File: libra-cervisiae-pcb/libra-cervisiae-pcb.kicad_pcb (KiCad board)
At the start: 2 copper layers, 63.8 x 43.2 mm, 161 parts, among them CN1 CP2102-BREAKOUT, CN3 HX711_BREAKOUT, J1 Board Temp, J10 Load Cell, J12 Load Cell, J4 Wort Temp, J8 Load Cell, J9 Load Cell, SW1 Reset, SW2 Flash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

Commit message: Versioning, silkscreen changes
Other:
- board text added: "0.1.0"
- board text added: "Load Cells"
- board text removed: "1.0.0"
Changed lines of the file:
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@@
   (general
     (thickness 1.6)
-    (drawings 12)
+    (drawings 14)
     (tracks 342)
     (zones 0)
@@
   (title_block
     (title "Libra Cervisiae PCB")
-    (date 2018-07-19)
-    (rev 1.0.0-rc.1)
+    (date 2018-07-23)
+    (rev 0.1.0)
   )
   (layers
@@
     (aux_axis_origin 11.938 11.938)
     (grid_origin 160.909 81.534)
-    (visible_elements FFFFFFFF)
+    (visible_elements FFFFEFFF)
     (pcbplotparams
       (layerselection 0x010fc_ffffffff)
@@
       (effects (font (size 1 1) (thickness 0.15)))
     )
-    (fp_text value "Load Cell" (at -9.779 -2.286 180) (layer F.SilkS)
+    (fp_text value "Load Cell" (at 1.8415 5.6515 180) (layer F.Fab)
       (effects (font (size 1 1) (thickness 0.15)))
     )
@@
     )
   )
+  (gr_line (start 139.954 88.025) (end 139.954 73.025) (angle 90) (layer F.SilkS) (width 0.2))
+  (gr_text "Load Cells" (at 136.017 69.723 90) (layer F.SilkS)
+    (effects (font (size 1 1) (thickness 0.15)))
+  )
   (gr_text "GRN/WHT +/-S\nBLK/RED -/+E" (at 152.908 59.309) (layer Cmts.User)
     (effects (font (size 1 1) (thickness 0.15)))
   )
   (gr_line (start 163.216 73.025) (end 139.954 73.025) (angle 90) (layer F.SilkS) (width 0.2))
-  (gr_line (start 163.195 88.152) (end 163.195 73.152) (angle 90) (layer F.SilkS) (width 0.2))
+  (gr_line (start 163.195 88.025) (end 163.195 73.025) (angle 90) (layer F.SilkS) (width 0.2))
   (dimension 64 (width 0.3) (layer Dwgs.User)
     (gr_text "64.000 mm" (at 138.138 59.988) (layer Dwgs.User)
@@
     (arrow2b (pts (xy 100.138 111.738) (xy 101.264504 111.151579)))
   )
-  (gr_text 1.0.0 (at 126.873 82.931) (layer F.SilkS)
+  (gr_text 0.1.0 (at 126.873 82.931) (layer F.SilkS)
     (effects (font (size 1 1) (thickness 0.15)))
   )

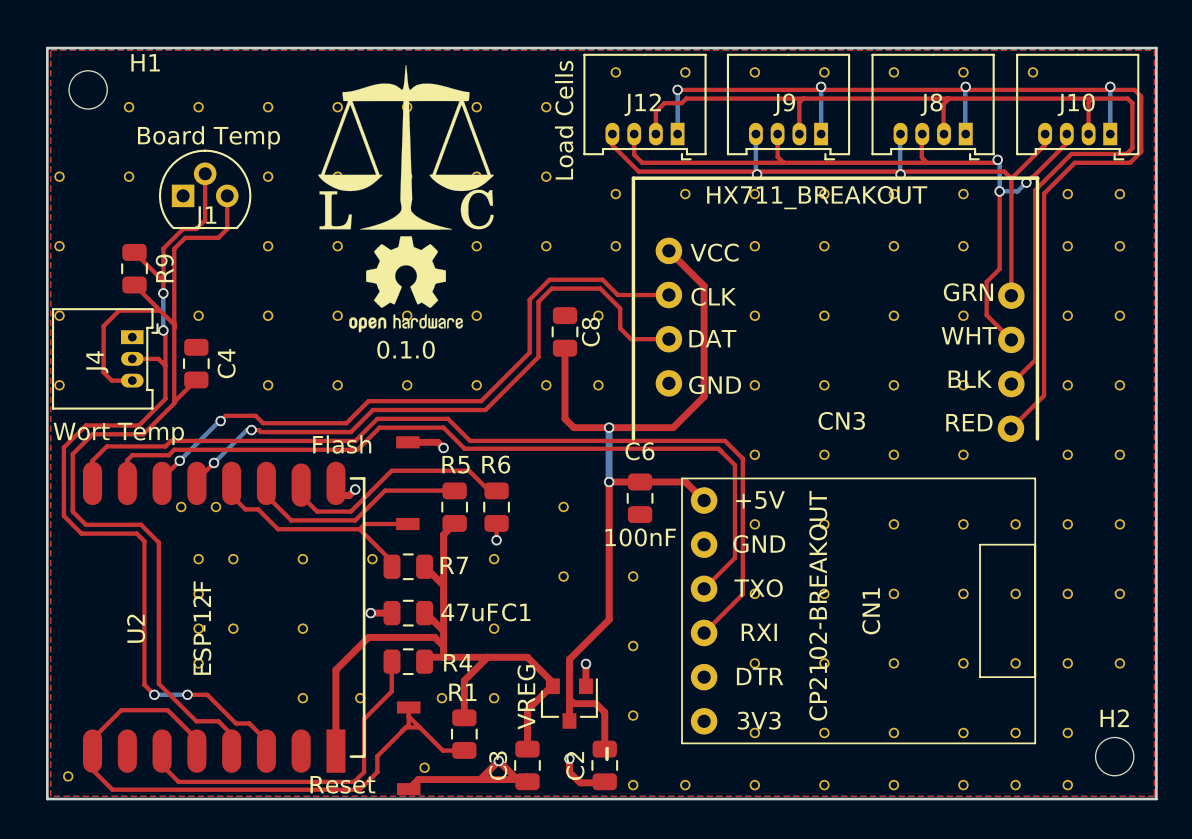
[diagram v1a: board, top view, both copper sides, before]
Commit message: Some PCB tweaks based on measuring the breakout boards
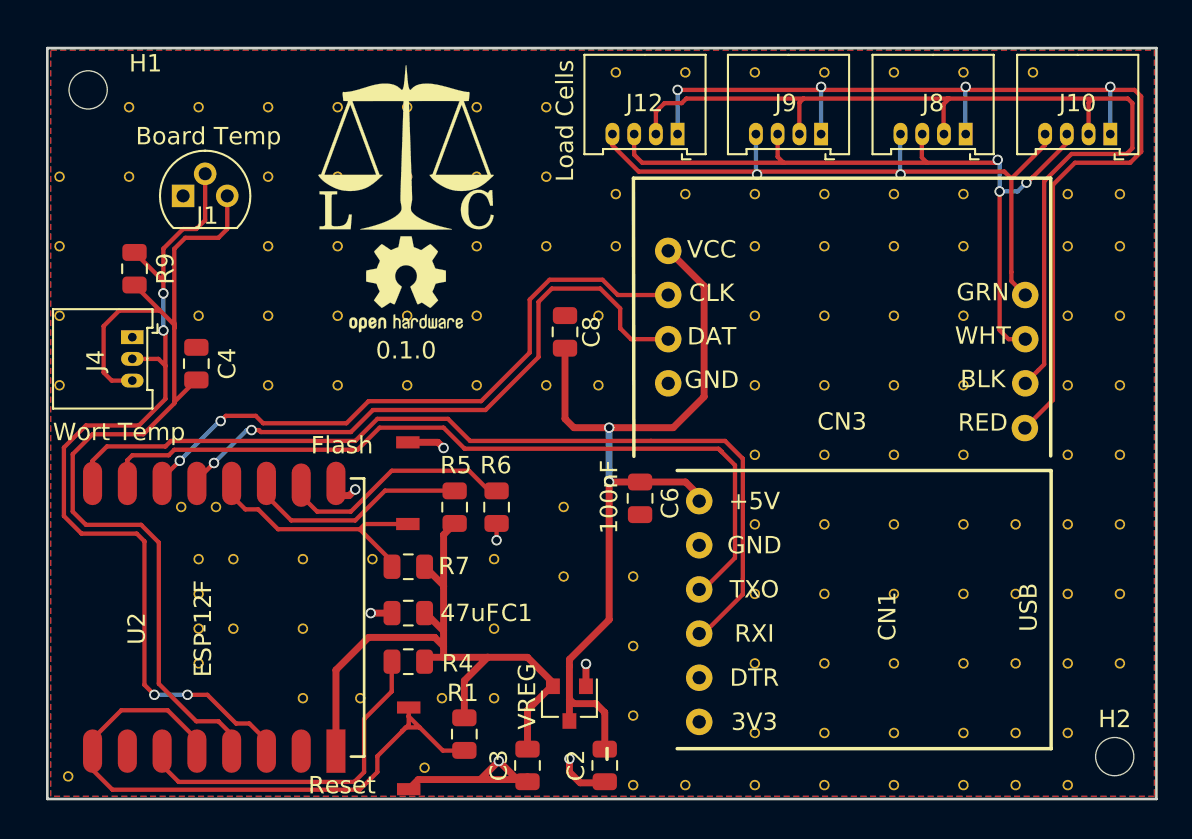
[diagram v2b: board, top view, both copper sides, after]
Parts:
- CN1: value CP2102-BREAKOUT -> CP2102
- moved CN1 0.94 mm to (164.0, 105.8)

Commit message: PCB cleanup (tracks, lines)
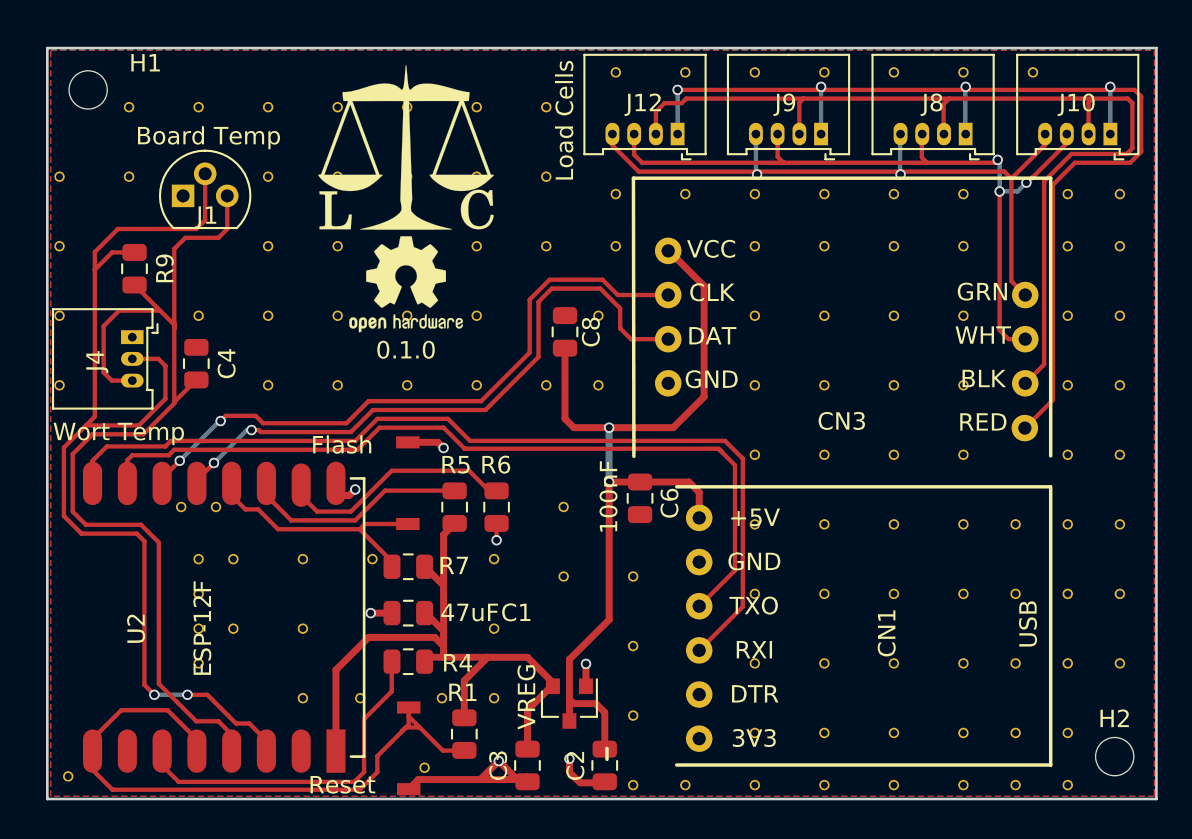
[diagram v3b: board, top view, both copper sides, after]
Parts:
- moved CN1 0.97 mm to (164.0, 106.8)
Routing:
- net /DSD: track 52.7 -> 60.5 mm, vias 4 -> 2
- net /HostRX: track 52.3 -> 53.4 mm
- net /HostTX: track 48.2 -> 49.3 mm
- net /USB+: track 50.5 -> 51.5 mm

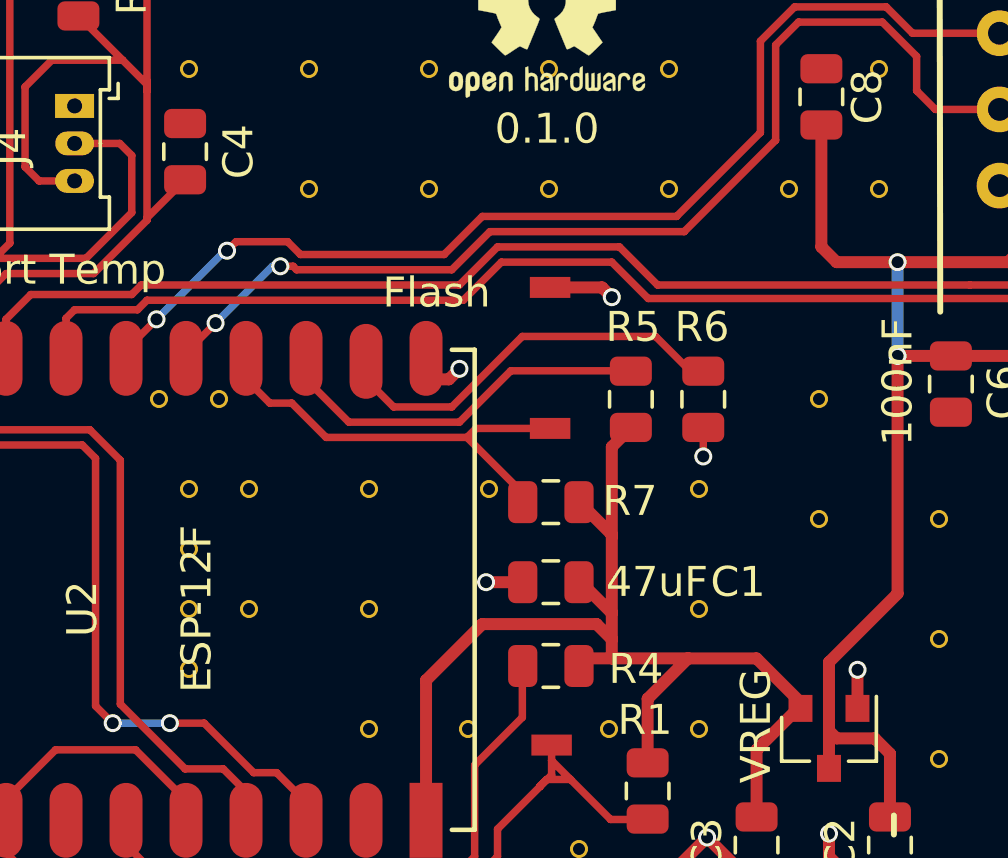
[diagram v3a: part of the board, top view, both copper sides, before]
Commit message: PCB stitching via tweaks
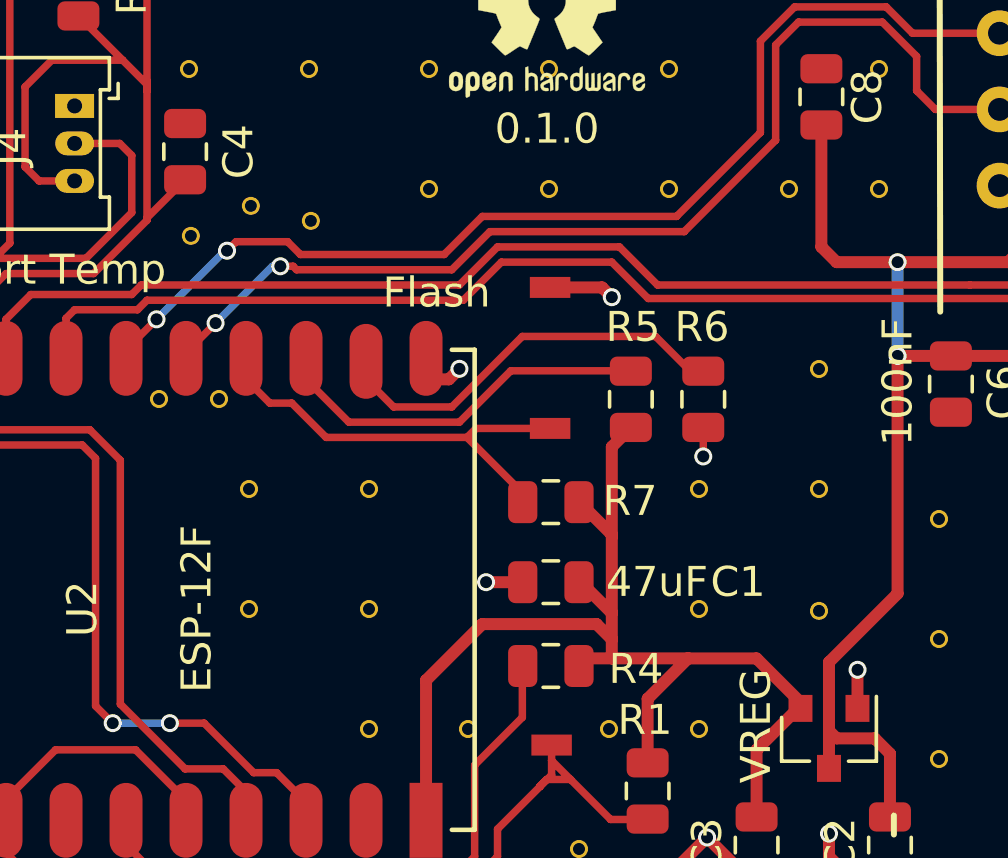
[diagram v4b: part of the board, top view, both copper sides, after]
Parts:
- removed the REF** at (124.9, 94.9)
- removed the REF** at (118.9, 84.9)
- removed the REF** at (114.9, 98.9)
- removed the REF** at (114.9, 100.9)
- removed the REF** at (114.9, 96.9)
- removed the REF** at (114.9, 94.9)
- added REF**: Stitch, Extra_Pads:Stitching_Via_0.6mm, F.Cu at (119.0, 86.0)
- added REF**: Stitch, Extra_Pads:Stitching_Via_0.6mm, F.Cu at (117.0, 85.5)
- added REF**: Stitch, Extra_Pads:Stitching_Via_0.6mm, F.Cu at (115.0, 86.5)
- added REF**: Stitch, Extra_Pads:Stitching_Via_0.6mm, F.Cu at (135.9, 99.0)
- moved REF** 1.00 mm to (135.9, 94.9)
- moved REF** 1.00 mm to (135.9, 90.9)
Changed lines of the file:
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@@
     (tracks 336)
     (zones 0)
-    (modules 161)
+    (modules 159)
     (nets 19)
   )
@@
     (add_net "Net-(R6-Pad2)")
   )
+  (module Extra_Pads:Stitching_Via_0.6mm (layer F.Cu)
+    (at 119 86)
+    (fp_text reference REF** (at 0 0.1) (layer F.SilkS) hide
+      (effects (font (size 0.25 0.25) (thickness 0.025)))
+    )
+    (fp_text value Stitch (at 0 -0.1) (layer F.Fab) hide
+      (effects (font (size 0.25 0.25) (thickness 0.025)))
+    )
+    (pad 1 thru_hole circle (at 0 0) (size 0.6 0.6) (drill 0.4) (layers *.Cu)
+      (net 6 /GND) (zone_connect 2))
+  )
+  (module Extra_Pads:Stitching_Via_0.6mm (layer F.Cu)
+    (at 117 85.5)
+    (fp_text reference REF** (at 0 0.1) (layer F.SilkS) hide
+      (effects (font (size 0.25 0.25) (thickness 0.025)))
+    )
+    (fp_text value Stitch (at 0 -0.1) (layer F.Fab) hide
+      (effects (font (size 0.25 0.25) (thickness 0.025)))
+    )
+    (pad 1 thru_hole circle (at 0 0) (size 0.6 0.6) (drill 0.4) (layers *.Cu)
+      (net 6 /GND) (zone_connect 2))
+  )
+  (module Extra_Pads:Stitching_Via_0.6mm (layer F.Cu)
+    (at 115 86.5)
+    (fp_text reference REF** (at 0 0.1) (layer F.SilkS) hide
+      (effects (font (size 0.25 0.25) (thickness 0.025)))
+    )
+    (fp_text value Stitch (at 0 -0.1) (layer F.Fab) hide
+      (effects (font (size 0.25 0.25) (thickness 0.025)))
+    )
+    (pad 1 thru_hole circle (at 0 0) (size 0.6 0.6) (drill 0.4) (layers *.Cu)
+      (net 6 /GND) (zone_connect 2))
+  )
+  (module Extra_Pads:Stitching_Via_0.6mm (layer F.Cu)
+    (at 135.938 99)
+    (fp_text reference REF** (at 0 0.1) (layer F.SilkS) hide
+      (effects (font (size 0.25 0.25) (thickness 0.025)))
+    )
+    (fp_text value Stitch (at 0 -0.1) (layer F.Fab) hide
+      (effects (font (size 0.25 0.25) (thickness 0.025)))
+    )
+    (pad 1 thru_hole circle (at 0 0) (size 0.6 0.6) (drill 0.4) (layers *.Cu)
+      (net 6 /GND) (zone_connect 2))
+  )
   (module CP2102-BRK:CP2102-BREAKOUT (layer F.Cu)
     (at 163.957 106.807 180)
@@
   (module Extra_Pads:Stitching_Via_0.6mm (layer F.Cu)
     (at 118.938 80.938)
-    (fp_text reference REF** (at 0 0.1) (layer F.SilkS) hide
-      (effects (font (size 0.25 0.25) (thickness 0.025)))
-    )
-    (fp_text value Stitch (at 0 -0.1) (layer F.Fab) hide
-      (effects (font (size 0.25 0.25) (thickness 0.025)))
-    )
-    (pad 1 thru_hole circle (at 0 0) (size 0.6 0.6) (drill 0.4) (layers *.Cu)
-      (net 6 /GND) (zone_connect 2))
-  )
-  (module Extra_Pads:Stitching_Via_0.6mm (layer F.Cu)
-    (at 118.938 84.938)
     (fp_text reference REF** (at 0 0.1) (layer F.SilkS) hide
       (effects (font (size 0.25 0.25) (thickness 0.025)))
@@
   )
   (module Extra_Pads:Stitching_Via_0.6mm (layer F.Cu)
-    (at 135.938 95.938)
-    (fp_text reference REF** (at 0 0.1) (layer F.SilkS) hide
-      (effects (font (size 0.25 0.25) (thickness 0.025)))
-    )
-    (fp_text value Stitch (at 0 -0.1) (layer F.Fab) hide
-      (effects (font (size 0.25 0.25) (thickness 0.025)))
-    )
-    (pad 1 thru_hole circle (at 0 0) (size 0.6 0.6) (drill 0.4) (layers *.Cu)
-      (net 6 /GND) (zone_connect 2))
-  )
-  (module Extra_Pads:Stitching_Via_0.6mm (layer F.Cu)
-    (at 135.938 91.938)
+    (at 135.938 94.938)
+    (fp_text reference REF** (at 0 0.1) (layer F.SilkS) hide
+      (effects (font (size 0.25 0.25) (thickness 0.025)))
+    )
+    (fp_text value Stitch (at 0 -0.1) (layer F.Fab) hide
+      (effects (font (size 0.25 0.25) (thickness 0.025)))
+    )
+    (pad 1 thru_hole circle (at 0 0) (size 0.6 0.6) (drill 0.4) (layers *.Cu)
+      (net 6 /GND) (zone_connect 2))
+  )
+  (module Extra_Pads:Stitching_Via_0.6mm (layer F.Cu)
+    (at 135.938 90.938)
     (fp_text reference REF** (at 0 0.1) (layer F.SilkS) hide
       (effects (font (size 0.25 0.25) (thickness 0.025)))
@@
   (module Extra_Pads:Stitching_Via_0.6mm (layer F.Cu)
     (at 116.938 98.938)
-    (fp_text reference REF** (at 0 0.1) (layer F.SilkS) hide
-      (effects (font (size 0.25 0.25) (thickness 0.025)))
-    )
-    (fp_text value Stitch (at 0 -0.1) (layer F.Fab) hide
-      (effects (font (size 0.25 0.25) (thickness 0.025)))
-    )
-    (pad 1 thru_hole circle (at 0 0) (size 0.6 0.6) (drill 0.4) (layers *.Cu)
-      (net 6 /GND) (zone_connect 2))
-  )
-  (module Extra_Pads:Stitching_Via_0.6mm (layer F.Cu)
-    (at 114.938 98.938)
-    (fp_text reference REF** (at 0 0.1) (layer F.SilkS) hide
-      (effects (font (size 0.25 0.25) (thickness 0.025)))
-    )
-    (fp_text value Stitch (at 0 -0.1) (layer F.Fab) hide
-      (effects (font (size 0.25 0.25) (thickness 0.025)))
-    )
-    (pad 1 thru_hole circle (at 0 0) (size 0.6 0.6) (drill 0.4) (layers *.Cu)
-      (net 6 /GND) (zone_connect 2))
-  )
-  (module Extra_Pads:Stitching_Via_0.6mm (layer F.Cu)
-    (at 114.938 100.938)
-    (fp_text reference REF** (at 0 0.1) (layer F.SilkS) hide
-      (effects (font (size 0.25 0.25) (thickness 0.025)))
-    )
-    (fp_text value Stitch (at 0 -0.1) (layer F.Fab) hide
-      (effects (font (size 0.25 0.25) (thickness 0.025)))
-    )
-    (pad 1 thru_hole circle (at 0 0) (size 0.6 0.6) (drill 0.4) (layers *.Cu)
-      (net 6 /GND) (zone_connect 2))
-  )
-  (module Extra_Pads:Stitching_Via_0.6mm (layer F.Cu)
-    (at 114.938 96.938)
-    (fp_text reference REF** (at 0 0.1) (layer F.SilkS) hide
-      (effects (font (size 0.25 0.25) (thickness 0.025)))
-    )
-    (fp_text value Stitch (at 0 -0.1) (layer F.Fab) hide
-      (effects (font (size 0.25 0.25) (thickness 0.025)))
-    )
-    (pad 1 thru_hole circle (at 0 0) (size 0.6 0.6) (drill 0.4) (layers *.Cu)
-      (net 6 /GND) (zone_connect 2))
-  )
-  (module Extra_Pads:Stitching_Via_0.6mm (layer F.Cu)
-    (at 114.938 94.938)
     (fp_text reference REF** (at 0 0.1) (layer F.SilkS) hide
       (effects (font (size 0.25 0.25) (thickness 0.025)))
@@
     (fp_text reference REF** (at 0 0.1) (layer F.SilkS) hide
       (effects (font (size 0.25 0.25) (thickness 0.025)))
-    )
-    (fp_text value Stitch (at 0 -0.1) (layer F.Fab) hide
-      (effects (font (size 0.25 0.25) (thickness 0.025)))
-    )
-    (pad 1 thru_hole circle (at 0 0) (size 0.6 0.6) (drill 0.4) (layers *.Cu)
-      (net 6 /GND) (zone_connect 2))
-  )
-  (module Extra_Pads:Stitching_Via_0.6mm (layer F.Cu)
-    (at 124.938 94.938)
-    (fp_text reference REF** (at 0 0.1) (layer F.SilkS) hide
-      (effects (font (size 0.25 0.25) (thickness 0.025)))
